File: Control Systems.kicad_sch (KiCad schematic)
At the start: 117 parts, among them J1 XT60-M, J10 Battery input, J11 Canbus, J12 Conn_02x03_Odd_Even, J13 USB_RX/TX, J14 Conn_01x08_Socket, J15 Conn_01x08_Socket, J16 Conn_01x03_Pin, J2 10118194-0001LF, J3 Conn_01x03_Pin, J4 Conn_01x03_Pin, J5 Conn_01x03_Pin, J7 USB_RX/TX, J8 MEM2061-01-188-00-A_REVA, J9 5-1814832-2, Q1 CSD18504Q5A, Q2 CSD18504Q5A, U1 STM32F446RETx, U10 TPS2121RUXR, U11 MMC5983MA, U2 LSM6DSL, U3 BMI088, U5 NEO-M8N-0, U6 TL1963A-33DCYR, U7 TPS552882QWRPMRQ1, U8 USBLC6-2SC6, U9 TPS1H200AQDGNRQ1, Y1 SIT8924BA-20.0

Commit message: Placement of components and initial VIA placement
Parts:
- removed C6: 100n, Capacitor_SMD:C_0402_1005Metric, symbol Device:C
- removed D10, D11, D15, D8, D9: TVS, Diode_SMD:Nexperia_DSN1608-2_1.6x0.8mm, symbol Diode:PTVS10VZ1USK
- removed D12, D13, D14, D7: SMAJ6.0CA, Diode_SMD:D_SMA, symbol Diode:SMAJ6.0CA
- removed J10: Battery input, Connector_Wago:Wago_734-162_1x02_P3.50mm_Horizontal, symbol Connector:Screw_Terminal_01x02
- removed J11: Canbus, Connector_Wago:Wago_734-163_1x03_P3.50mm_Horizontal, symbol Connector:Screw_Terminal_01x03
- added C13, C39: 1u, Capacitor_SMD:C_0402_1005Metric, symbol Device:C
- added C14: 100n, Capacitor_SMD:C_0402_1005Metric, symbol Device:C
- added D10, D14, D8, D9: SMAJ12A, Diode_SMD:D_SMA, symbol Diode:SMAJ12A
- added D11: SMAJ9.0A, Diode_SMD:D_SMA, symbol Diode:SMAJ9.0A
- added D12, D13, D23, D7: SD05_SOD323, Diode_SMD:D_SOD-323, symbol Diode:SD05_SOD323
- added FB2: 120R, Inductor_SMD:L_0603_1608Metric, symbol Device:FerriteBead
- added J10: Canbus, imports:CONN_SD-39357-001_03P_MOL, symbol 2025-12-18_17-37-14:393570003
- added J6: Battery input, imports:691137710002, symbol 691137710002:691137710002
- added MH1, MH2, MH3, MH4: M2, MountingHole:MountingHole_2.2mm_M2_Pad_Via, symbol Mechanical:MountingHole_Pad
- J14, J15: footprint Connector_PinSocket_2.54mm:PinSocket_1x08_P2.54mm_Vertical -> Connector_PinSocket_2.00mm:PinSocket_1x08_P2.00mm_Vertical
- J7: value USB_RX/TX -> GPIO
- R4: value 47k -> 4k7; footprint Resistor_SMD:R_0603_1608Metric -> Capacitor_SMD:C_0402_1005Metric
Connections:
- net +3.3V: now also C39.2, FB2.1; no longer U1.13 (VDDA)
- net CAN2_RX: now also J10.1
- net CAN2_TX: now also J10.2
- net CAN_INT: now also J10.3
- net GND: now also D10.2 (A2), D12.2 (A2), D13.2 (A2), D14.2 (A2), D23.2 (A2), D7.2 (A2), D8.2 (A2), D9.2 (A2)
- net GP_LED: no longer D17.2 (A), U1.36 (PB15)
- net MCU_NRST: now also J12.1 (Pin_1), R3.1; no longer J12.5 (Pin_5)
- net PWM_TIM3_CH1: now also D23.1 (A1)
- net PWM_TIM3_CH2: now also D7.1 (A1)
- net PWM_TIM3_CH3: now also D12.1 (A1)
- net PWM_TIM3_CH4: now also D13.1 (A1)
- net RX_LED: no longer D18.2 (A), U1.50 (PA15)
- net SPI1_CS_2: now also U3.5 (CSB2); no longer J15.5 (Pin_5)
- net SPI1_CS_3: now also J15.5 (Pin_5); no longer U3.5 (CSB2)
- net SYS_SWDIO: now also J12.5 (Pin_5); no longer J12.1 (Pin_1)
- net Servo +8.2V: now also D10.1 (A1), D14.1 (A1), D8.1 (A1), D9.1 (A1)
- net USART1_RX: no longer D21.2 (A2), J13.1 (Pin_1), U1.58 (PB6)
- net VIN_7.4V: now also D11.1 (A1)
- net SWR_SW1: now reaches C34.2, L2.1, Q1.1 (S), Q1.2 (S), Q1.3 (S), Q2.5 (D), U7.23 (SW1)
- net BOOT0: now reaches C10.1, R2.2
- net BOOT0: no longer R3.1
- net Batt_out: now reaches D19.1 (K), U10.7 (IN1), U10.7_1 (IN1)
- net Batt_out: now also J6.2
- net at D19.2 (A): now also J6.1
- net VCC_RF: now reaches R6.1, U5.9 (VCC_RF)
- new net: C13.1, C14.1, C39.1
- new net +3.3VA: C13.2, C14.2, FB2.2, U1.13 (VDDA)
- new net GP_LED_IO: D17.2 (A), U1.36 (PB15)
- new net RX_LED_GP: D18.2 (A), U1.50 (PA15)
- new net USART1_TX: D21.2 (A2), J13.1 (Pin_1), U1.58 (PB6)
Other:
- note removed: "VERIFY PI FILTER AND TVS DIODE"
- moved on the sheet: C10, C20, C7, D22, J14, J15, R2, R3

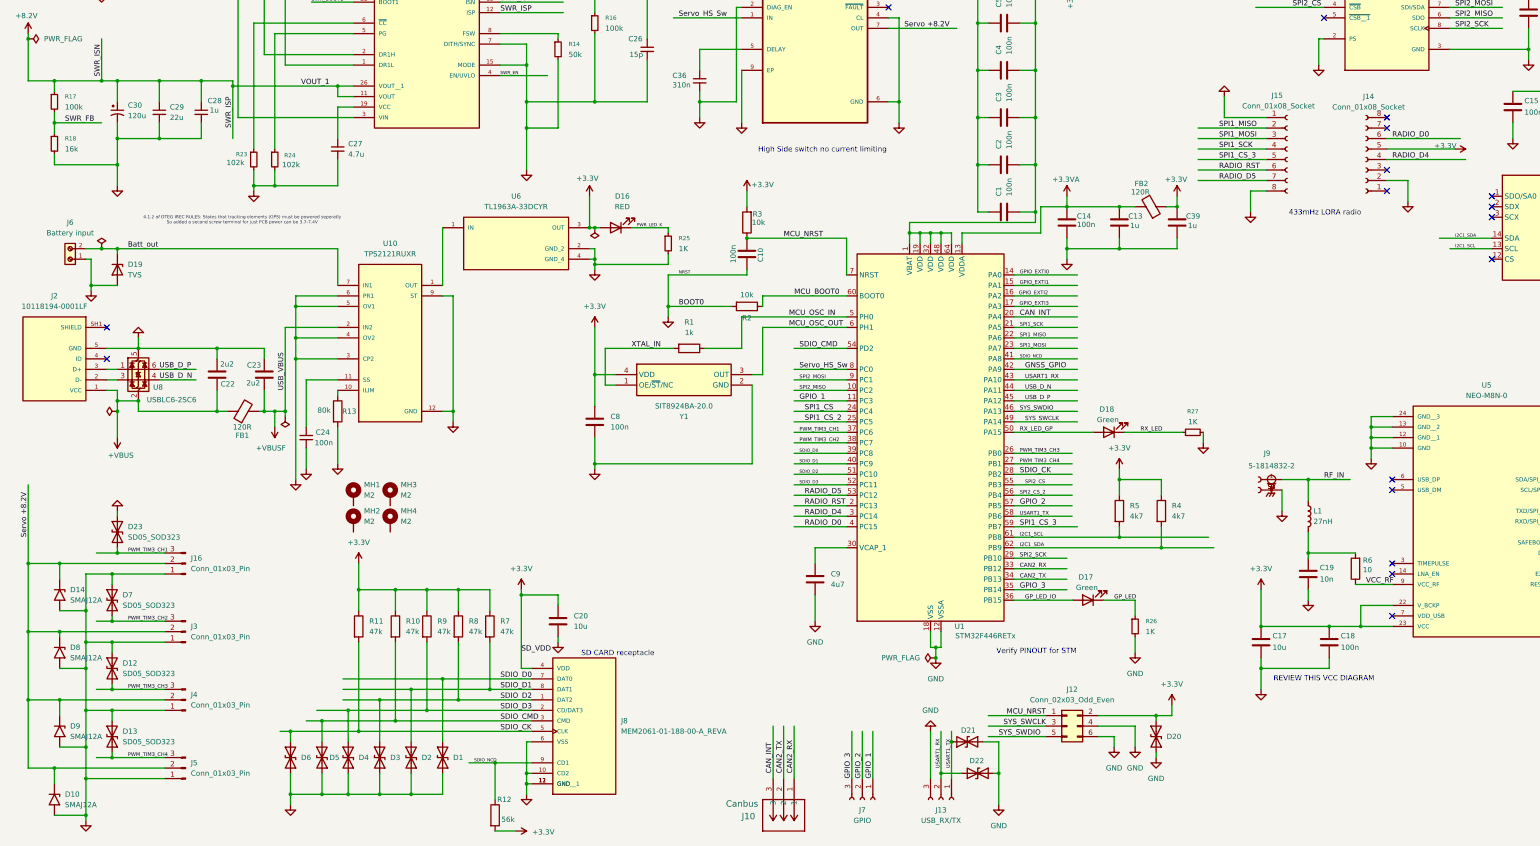
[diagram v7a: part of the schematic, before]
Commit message: Feat: VIAs placed and some routing
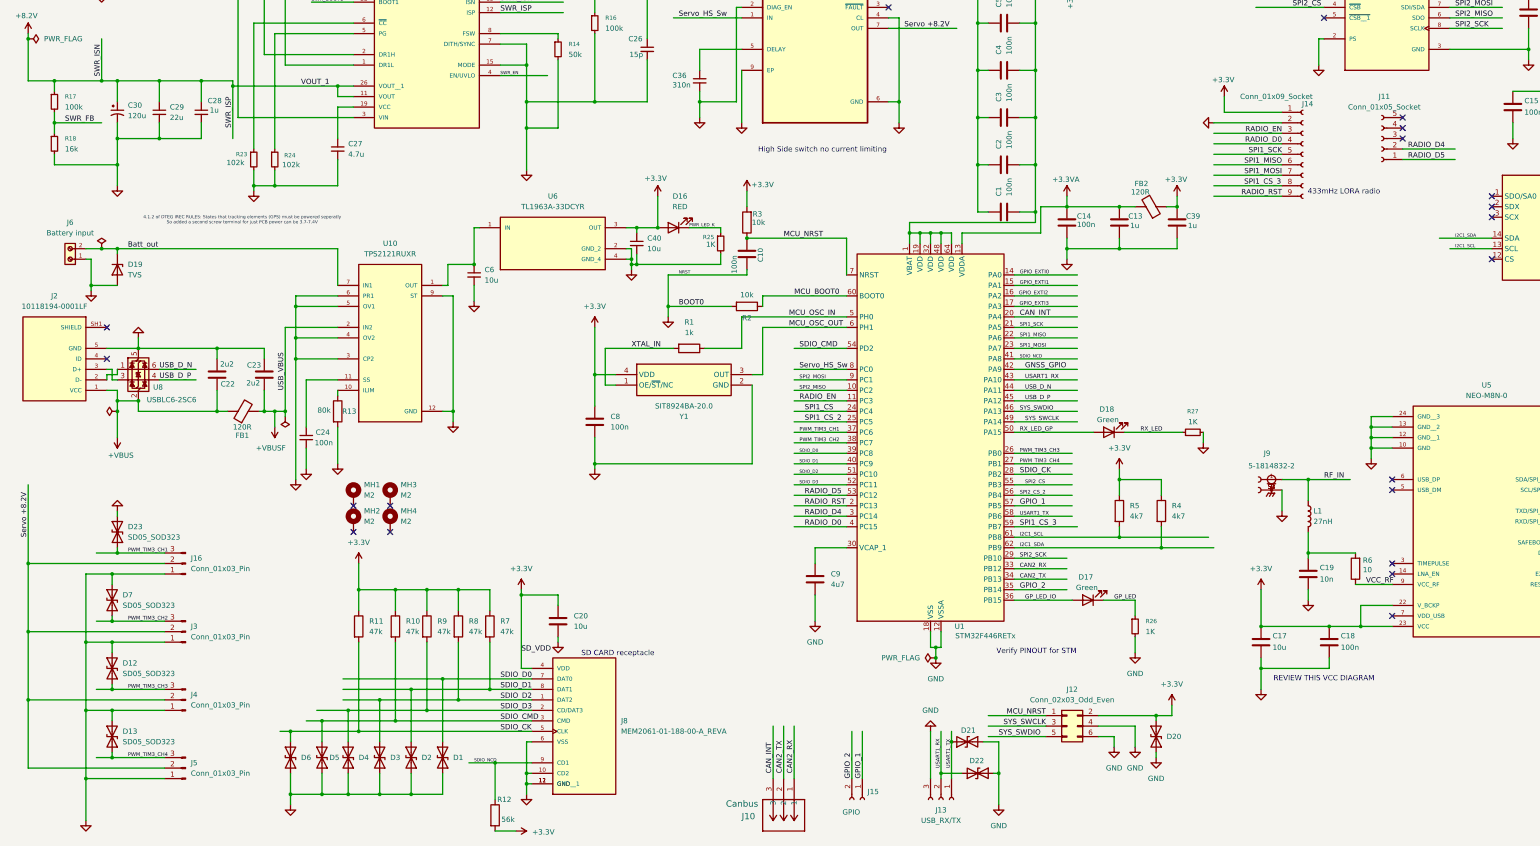
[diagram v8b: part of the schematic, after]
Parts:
- removed D10, D14, D8, D9: SMAJ12A, Diode_SMD:D_SMA, symbol Diode:SMAJ12A
- removed J14, J15: Conn_01x08_Socket, Connector_PinSocket_2.00mm:PinSocket_1x08_P2.00mm_Vertical, symbol Connector:Conn_01x08_Socket
- removed J7: GPIO, Connector_PinSocket_2.54mm:PinSocket_1x03_P2.54mm_Vertical, symbol Connector:Conn_01x03_Socket
- added C40, C6: 10u, Capacitor_SMD:C_0603_1608Metric, symbol Device:C_Small
- added J11: Conn_01x05_Socket, Connector_PinSocket_2.54mm:PinSocket_1x05_P2.54mm_Vertical, symbol Connector:Conn_01x05_Socket
- added J14: Conn_01x09_Socket, Connector_PinSocket_2.54mm:PinSocket_1x09_P2.54mm_Vertical, symbol Connector:Conn_01x09_Socket
- added J15: GPIO, Connector_PinSocket_2.54mm:PinSocket_1x02_P2.54mm_Vertical, symbol Connector:Conn_01x02_Socket
- C30: footprint Capacitor_SMD:C_0805_2012Metric -> Capacitor_SMD:CP_Elec_6.3x5.9
- C31: footprint Capacitor_SMD:C_0805_2012Metric -> Capacitor_SMD:CP_Elec_10x12.6
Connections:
- net GPIO_3 is gone; now on net GPIO_2: U1.35 (PB14)
- net +3.3V: now also C40.1, J14.1 (Pin_1)
- net GPIO_1: now also U1.57 (PB5), J15.1 (Pin_1); no longer U1.11 (PC3)
- net GPIO_2: now also J15.2 (Pin_2); no longer U1.57 (PB5)
- net RADIO_D0: now also J14.4 (Pin_4)
- net RADIO_D4: now also J11.2 (Pin_2)
- net RADIO_D5: now also J11.1 (Pin_1)
- net RADIO_RST: now also J14.9 (Pin_9)
- net SPI1_CS_3: now also J14.8 (Pin_8)
- net SPI1_MISO: now also J14.6 (Pin_6)
- net SPI1_MOSI: now also J14.7 (Pin_7)
- net SPI1_SCK: now also J14.5 (Pin_5)
- net USB_D_N: now also U8.6 (I/O1); no longer U8.4 (I/O2)
- net USB_D_P: now also U8.4 (I/O2); no longer U8.6 (I/O1)
- net at U10.1 (OUT), U10.1_1 (OUT), U10.8 (OUT)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: now also C6.1
- net at R25.2, U6.2 (GND_2), U6.4 (GND_4): now also C40.2
- net at J2.2 (D-): now also U8.1 (I/O1); no longer U8.3 (I/O2)
- net at J2.3 (D+): now also U8.3 (I/O2); no longer U8.1 (I/O1)
- new net RADIO_EN: J14.3 (Pin_3), U1.11 (PC3)
- no-connect marks 25 -> 28
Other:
- moved on the sheet: D16, R25, U6
